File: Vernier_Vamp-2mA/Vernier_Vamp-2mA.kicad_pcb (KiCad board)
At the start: 4 copper layers, 160 x 99.5 mm, 192 parts, among them J1 Conn_01x02, J2 RJ45, J3 Screw_Terminal_01x04, J4 Conn_02x07_Odd_Even, J5 Channel 3, J6 Channel 2, J7 Channel 1, Q1 Si4447ADY, Q2 IRF8707PbF, SW1 DPDT_Hirose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

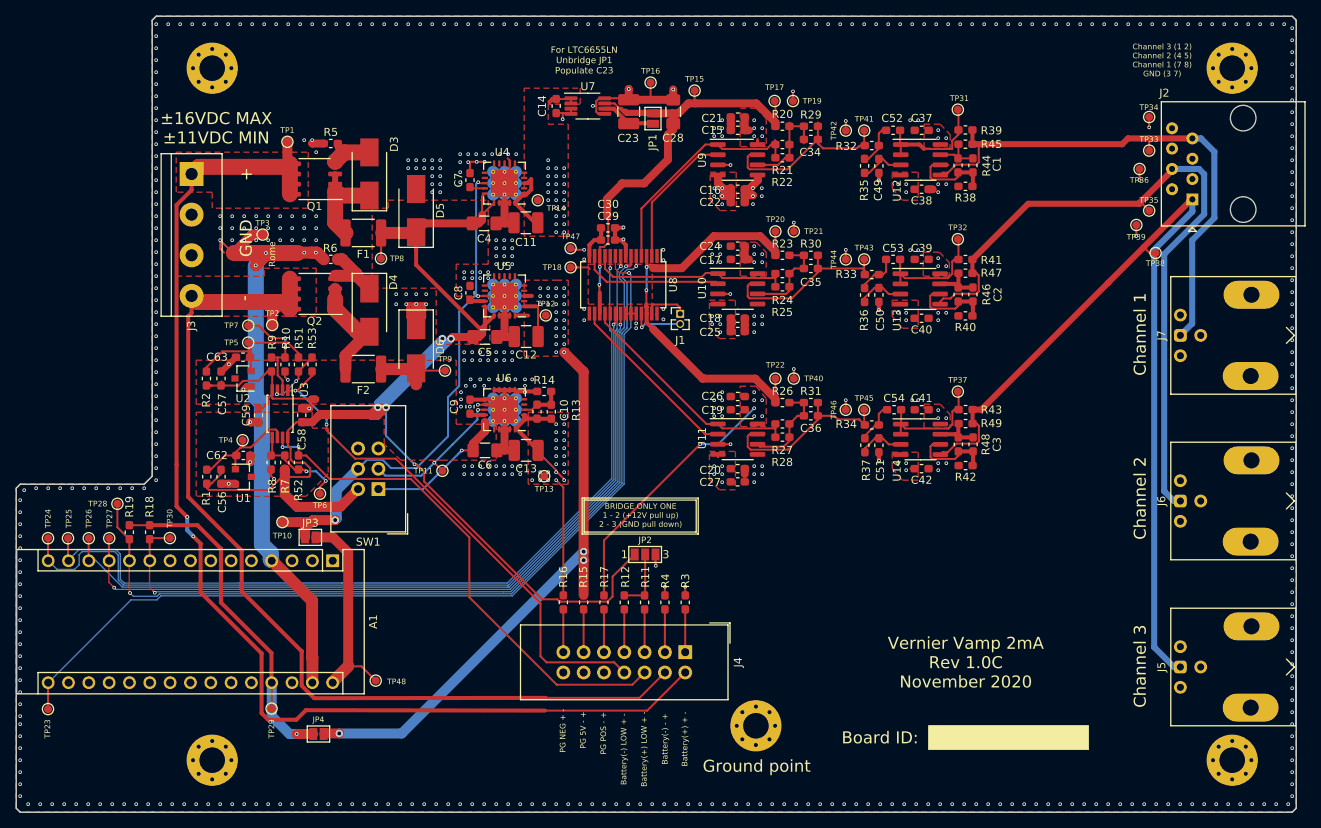
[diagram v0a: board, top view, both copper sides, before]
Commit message: Issue fixes
This commit, addresses following issues:
-Stray current at the output with only USB plugged in
-RFI Shield over analogue circuitry
-Wrong BNC connector footprint

Some general layout optimisation
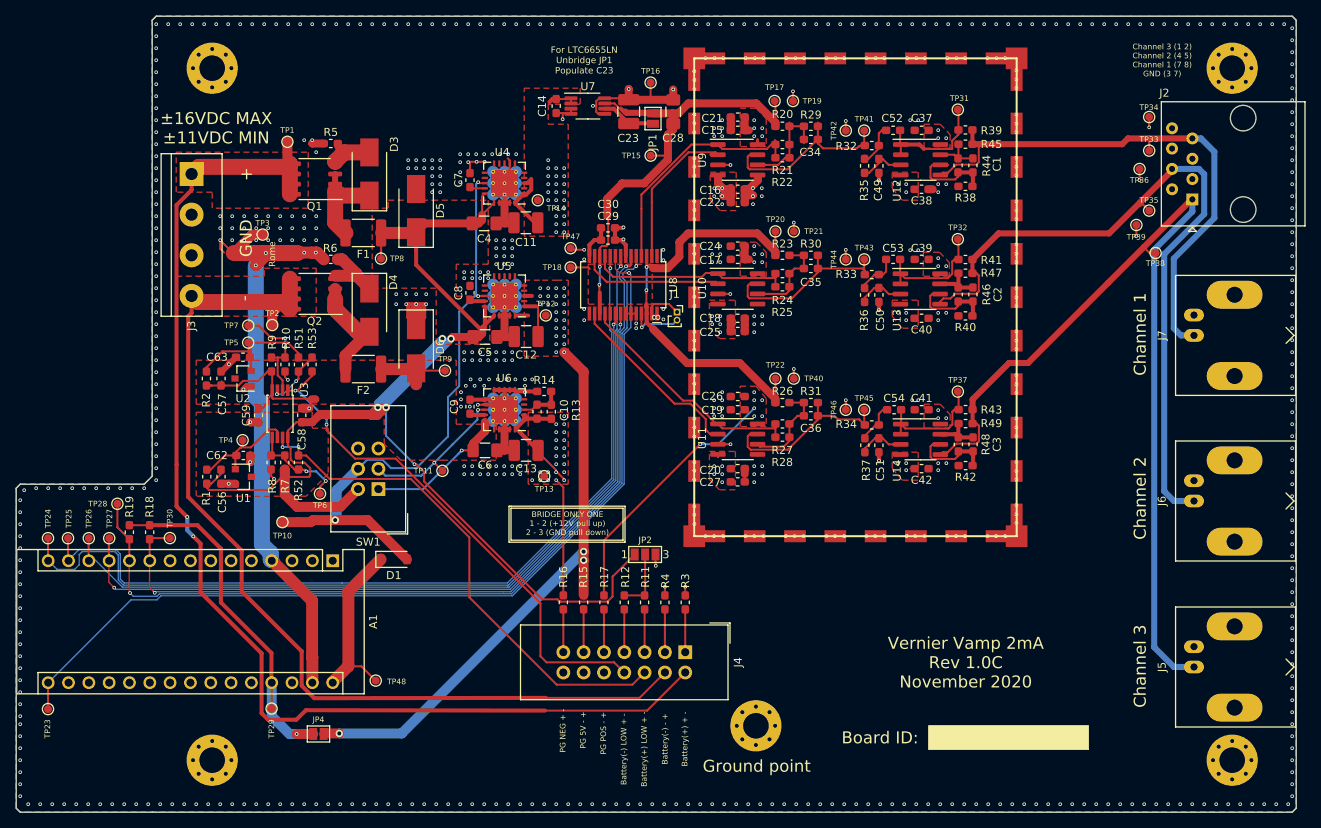
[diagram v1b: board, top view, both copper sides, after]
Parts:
- removed JP3: SolderJumper_2_Open, Jumper:SolderJumper-2_P1.3mm_Open_Pad1.0x1.5mm
- added D1: MBR0520LT, Diode_SMD:D_SOD-123, F.Cu at (80.1, 115.0)
- added J8: RF_Shield_Two_Pieces, MS548-10F:MS548-10C, F.Cu at (110.1, 85.0)
- J1: footprint Connector_PinHeader_1.27mm:PinHeader_1x02_P1.27mm_Vertical -> Connector_PinSocket_1.00mm:PinSocket_1x02_P1.00mm_Vertical
- J5, J6, J7: footprint Connector_Coaxial:BNC_Amphenol_031-6575_Horizontal -> Connector_Coaxial:BNC_Amphenol_B6252HB-NPP3G-50_Horizontal
- moved TP15 9.81 mm to (112.2, 64.6)
- moved J5 1.70 mm to (180.1, 128.5)
- moved J6 1.70 mm to (180.1, 107.8)
- moved J7 1.70 mm to (180.1, 87.0)
- moved J1 0.45 mm to (115.5, 84.1)
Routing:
- net +12V_batt_post: track 65.7 -> 74.5 mm
- net Net-(A1-Pad30): track 28.8 -> 24.8 mm
- net /Channel_Outputs/Coil_Iout_3: track 112.5 -> 115.0 mm
- net /Channel_Outputs/Coil_Iout_1: track 67.6 -> 69.9 mm
- net /DAC/Vref_2.5V: track 130.3 -> 132.4 mm
- net /Channel_Outputs/Coil_Iout_2: track 90.6 -> 92.3 mm
- net Net-(U8-Pad2): track 18.4 -> 19.6 mm
- net Net-(R21-Pad1): track 28.6 -> 29.6 mm
- net /DAC/Iout_D: track 5.47 -> 4.60 mm
- net Net-(U11-Pad2): track 22.4 -> 23.2 mm
- net GND: vias 566 -> 680

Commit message: Silkscreen fixes
Silkscreen settings changed so that references are not obstructed by the shield.
-Added magnetic field direction designation for each channel.
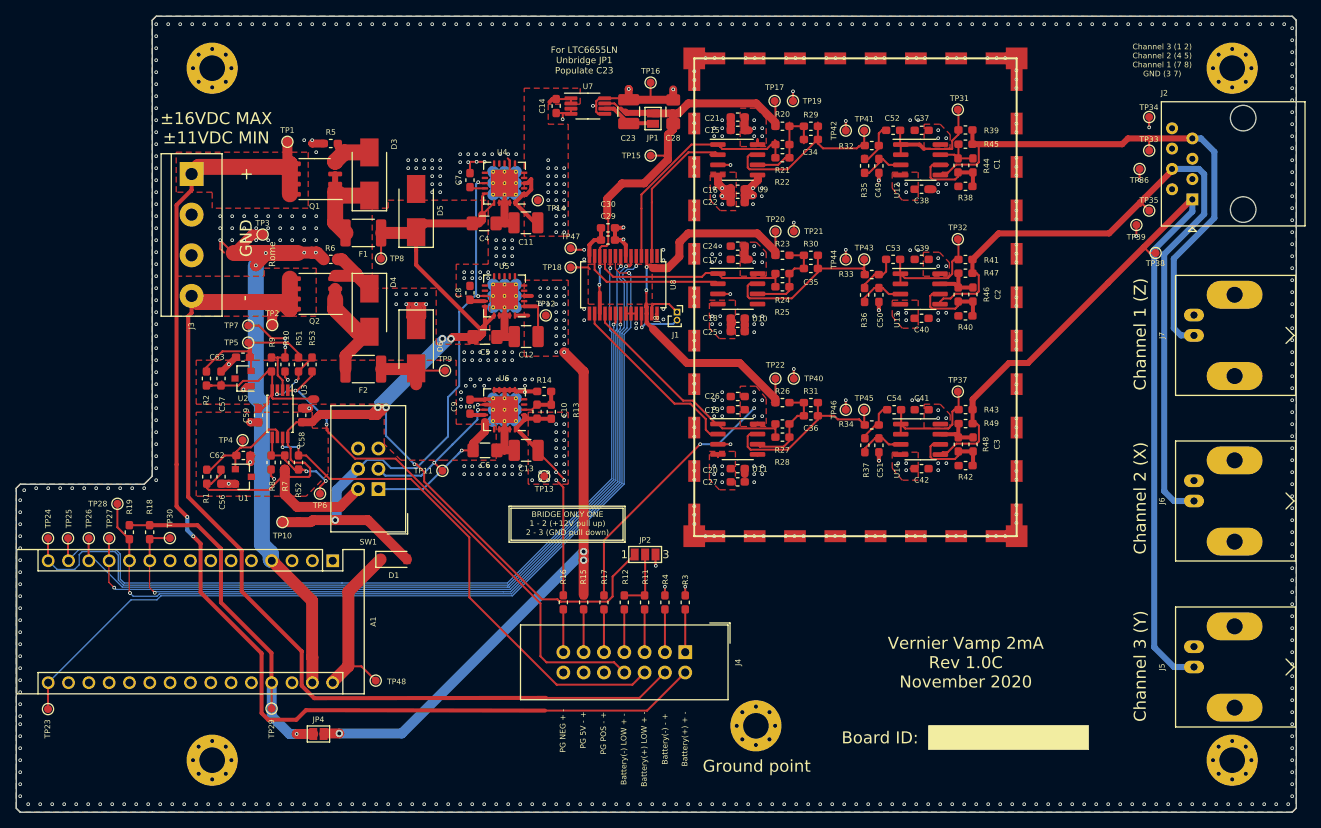
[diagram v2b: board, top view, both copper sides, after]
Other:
- board text added: "Channel 1 (Z)"
- board text added: "Channel 2 (X)"
- board text added: "Channel 3 (Y)"

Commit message: Change of J1 connector courtyard
PCB footprint change:
-J1 (1 mm pinheader) courtyard had been changed to pass DRC
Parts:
- J1: footprint Connector_PinSocket_1.00mm:PinSocket_1x02_P1.00mm_Vertical -> Dummy_conn_01x02:PinSocket_1x02_P1.00mm_Vertical_CUSTOM_CYD
- J8: value RF_Shield_Two_Pieces -> MS548-10F
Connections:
- A1 pad 1: (no net) -> Net-(A1-Pad1)
- A1 pad 17: (no net) -> Net-(A1-Pad17)
- A1 pad 18: (no net) -> Net-(A1-Pad18)
- A1 pad 19: (no net) -> Net-(A1-Pad19)
- A1 pad 2: (no net) -> Net-(A1-Pad2)
- A1 pad 20: (no net) -> Net-(A1-Pad20)
- A1 pad 21: (no net) -> Net-(A1-Pad21)
- A1 pad 22: (no net) -> Net-(A1-Pad22)
- A1 pad 23: (no net) -> Net-(A1-Pad23)
- A1 pad 24: (no net) -> Net-(A1-Pad24)
- A1 pad 25: (no net) -> Net-(A1-Pad25)
- A1 pad 26: (no net) -> Net-(A1-Pad26)
- A1 pad 28: (no net) -> Net-(A1-Pad28)
- A1 pad 3: (no net) -> Net-(A1-Pad3)
- A1 pad 5: (no net) -> Net-(A1-Pad5)
- A1 pad 6: (no net) -> Net-(A1-Pad6)
- A1 pad 7: (no net) -> Net-(A1-Pad7)
- A1 pad 8: (no net) -> Net-(A1-Pad8)
- A1 pad 9: (no net) -> Net-(A1-Pad9)
- U4 pad 11: (no net) -> Net-(U4-Pad11)
- U4 pad 4: (no net) -> Net-(U4-Pad4)
- U4 pad 5: (no net) -> Net-(U4-Pad5)
- U5 pad 11: (no net) -> Net-(U5-Pad11)
- U5 pad 12: (no net) -> Net-(U5-Pad12)
- U5 pad 4: (no net) -> Net-(U5-Pad4)
- U5 pad 5: (no net) -> Net-(U5-Pad5)
- U5 pad 8: (no net) -> Net-(U5-Pad8)
- U5 pad 9: (no net) -> Net-(U5-Pad9)

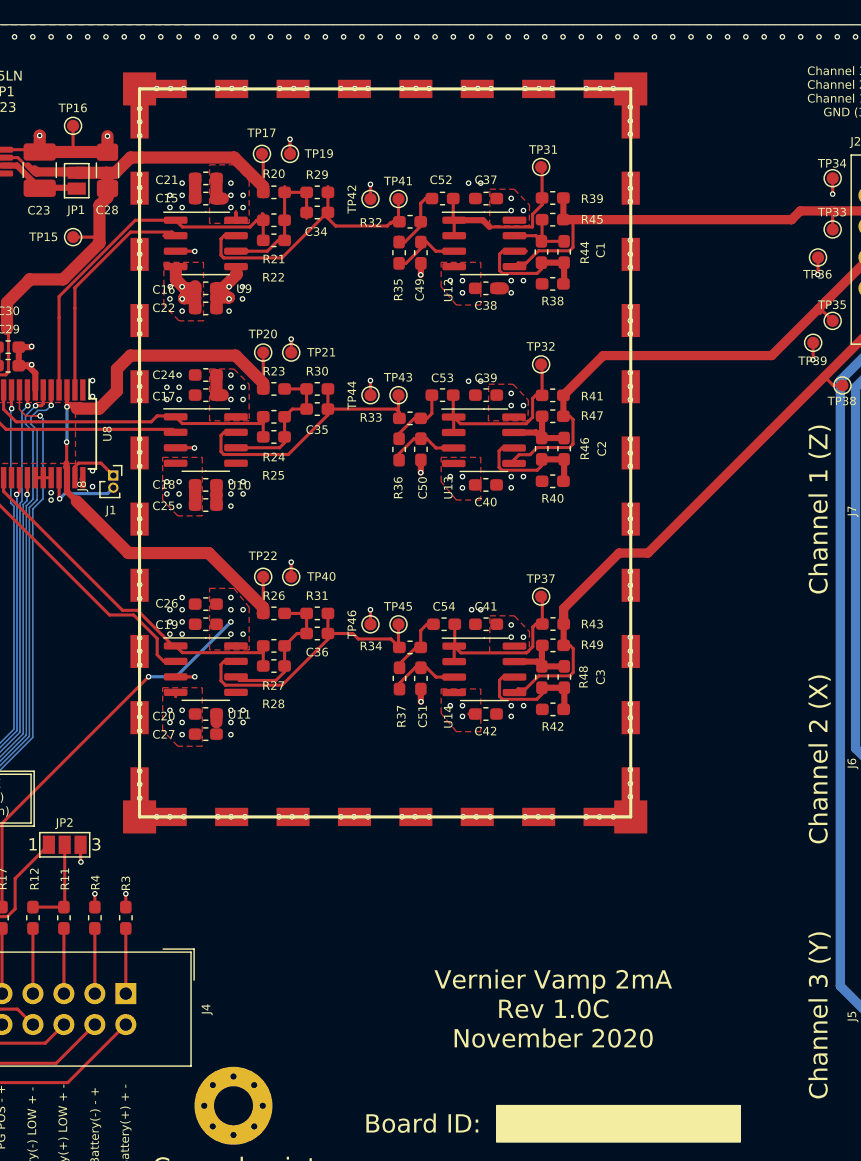
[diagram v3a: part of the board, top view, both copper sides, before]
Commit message: 2 mA changes
-2 mA version is now called "low current coil driver" LCCD
- Small changes to the PCB layout
- Shield footprint correction
- General optimisation
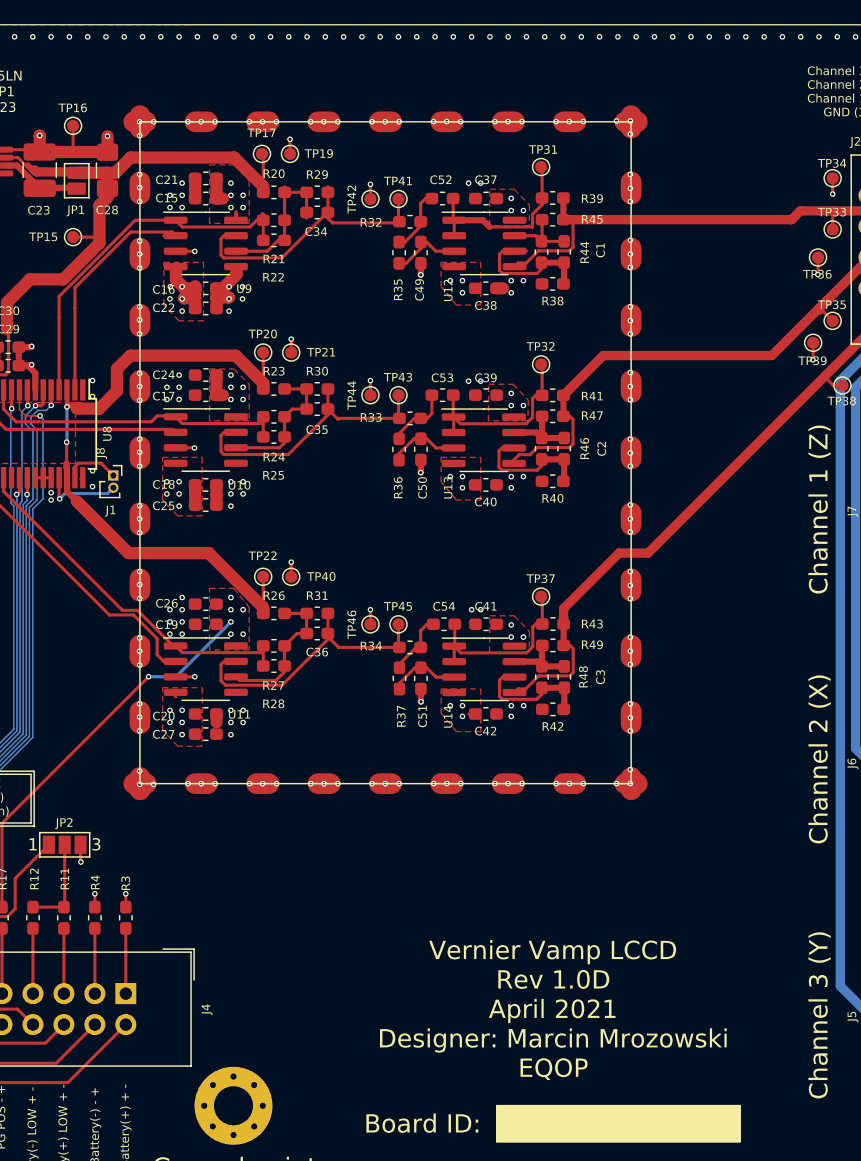
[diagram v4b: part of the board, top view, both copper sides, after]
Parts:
- moved J8 3.14 mm to (111.6, 82.3)
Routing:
- net /Channel_Outputs/4Q_DAC_OUT_2: track 23.6 -> 23.1 mm
- net GND: vias 680 -> 674
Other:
- board text added: "Vernier Vamp LCCD Rev 1.0D April 2021 Designer: Marcin Mrozowski EQOP"
- board text removed: "Vernier Vamp 2mA Rev 1.0C November 2020"
- board text removed: "Vernier Vamp 2mA Rev 1.0C November 2020 Designer: Marcin Mrozowski EQOP"

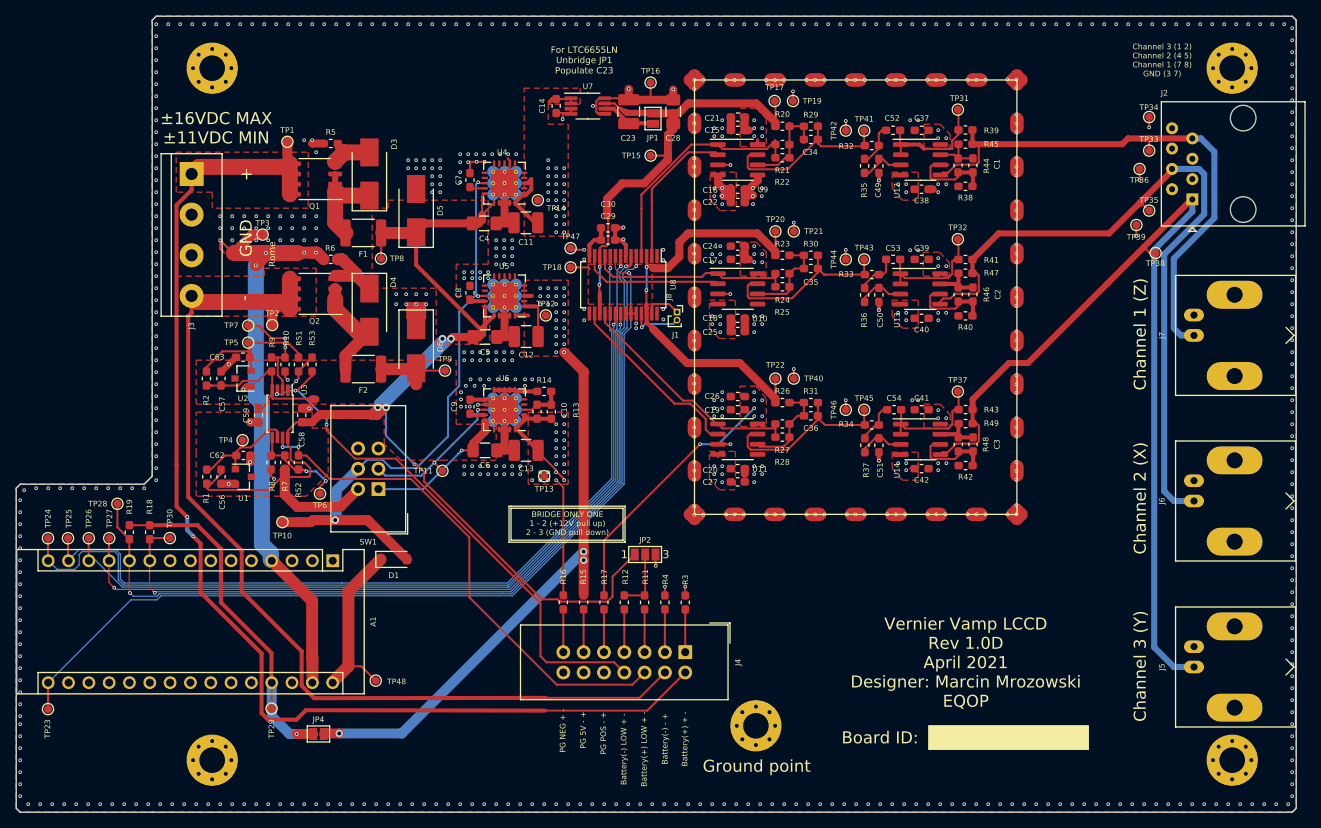
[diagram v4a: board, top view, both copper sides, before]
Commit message: 1.0D Update
LCCD changes
-Addition of trigger for calibration
-PCB optimisation

HCCD changes
-New output stage designed
-Changes from 1.0C applied to HCCD
-New more optimised layout
-New shielding over analog section
-Addition of trigger for calibration

New symbols and footprint creation
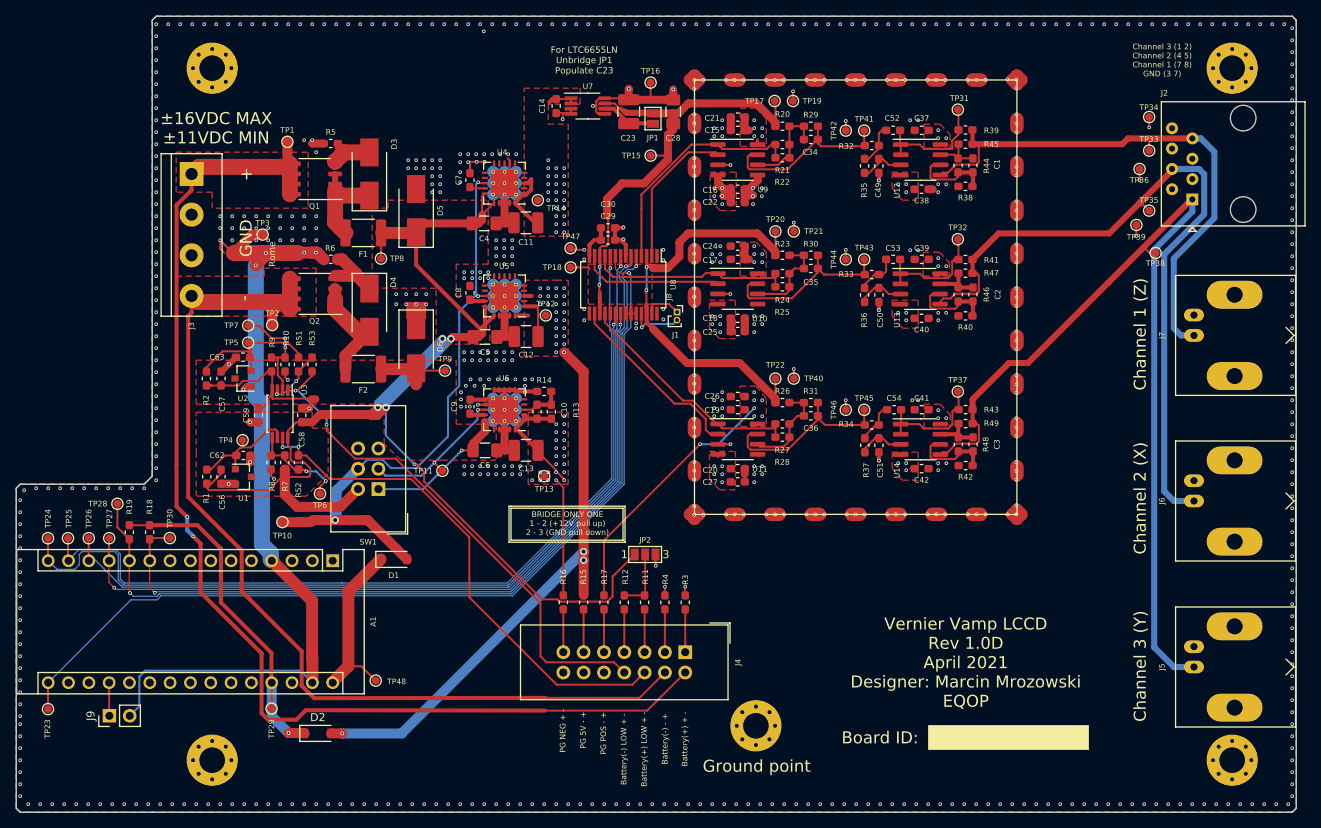
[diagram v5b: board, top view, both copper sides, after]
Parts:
- removed JP4: SolderJumper_2_Open, Jumper:SolderJumper-2_P1.3mm_Open_Pad1.0x1.5mm
- added D2: MBR0520LT, Diode_SMD:D_SOD-123, F.Cu at (70.6, 136.8)
- added J9: Conn_01x02, Connector_PinHeader_2.54mm:PinHeader_1x02_P2.54mm_Vertical, F.Cu at (44.5, 134.6)
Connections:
- A1 pad 19: Net-(A1-Pad19) -> /MCU/Trigger
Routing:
- net GNDD: track 57.2 -> 85.1 mm
- net /MCU/Trigger: track 0.00 -> 4.15 mm
- net Net-(C52-Pad1): track 16.3 -> 15.0 mm
- net +5VD: track 45.7 -> 44.8 mm
- net +5V: track 87.8 -> 87.0 mm
- net Net-(R21-Pad1): track 29.6 -> 29.0 mm
- net (no net): vias 0 -> 1
- removed copper zone on F.Cu, net (none)

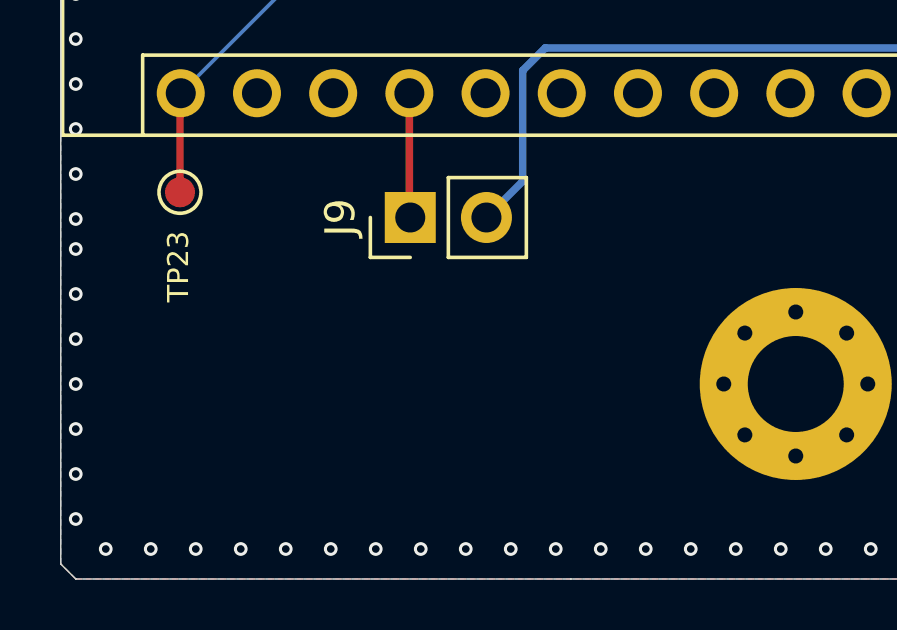
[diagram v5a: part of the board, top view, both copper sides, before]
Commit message: Addition of test points onto the bias circuitry
-Addition of test points onto the bias circuitry (HCCD)
-Silkscreen update (LCCD)
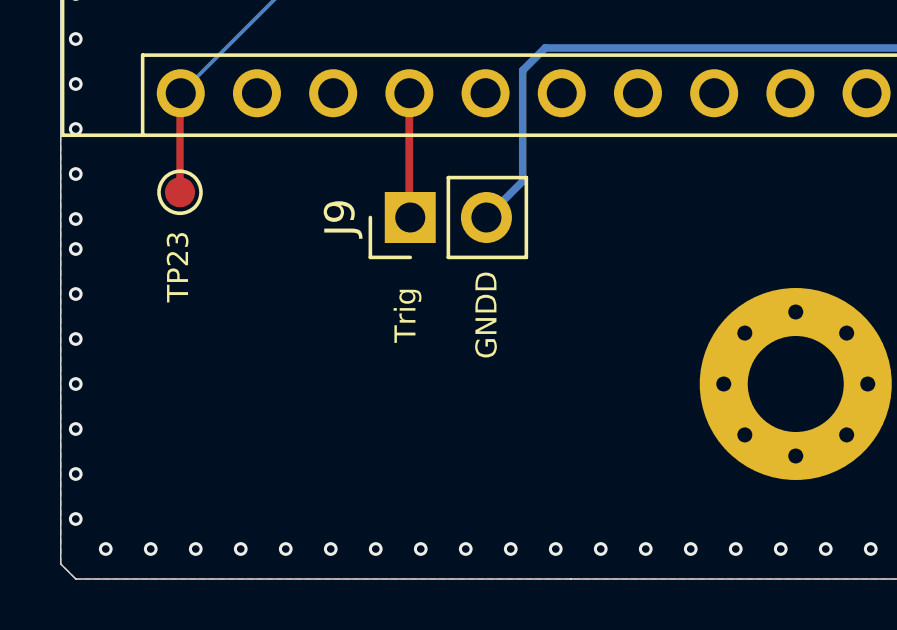
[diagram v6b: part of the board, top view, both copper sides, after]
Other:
- board text added: "GNDD"
- board text added: "Trig"
